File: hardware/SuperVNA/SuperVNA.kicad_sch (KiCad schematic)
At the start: 55 parts, among them Q101 2N2222, Q102 2N2222, U101 LM324, U102 AD626, U103 AD626, U104 SN74CBT3253, U105 SN74CBT3253

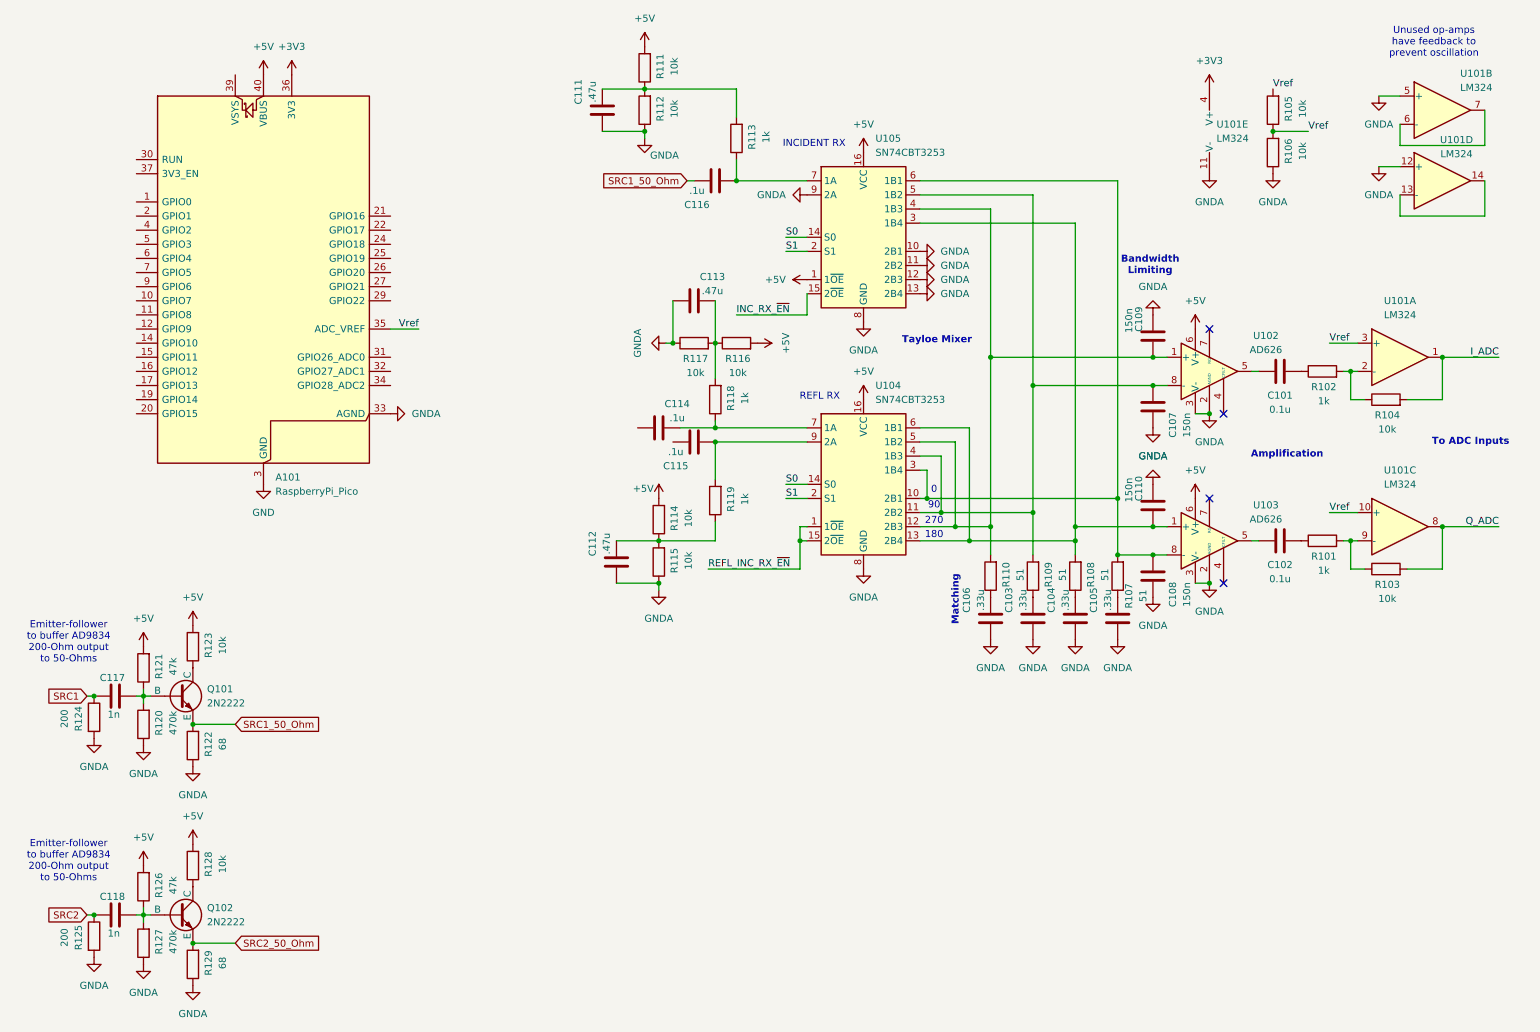
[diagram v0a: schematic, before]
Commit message: deal with the actual frequency used
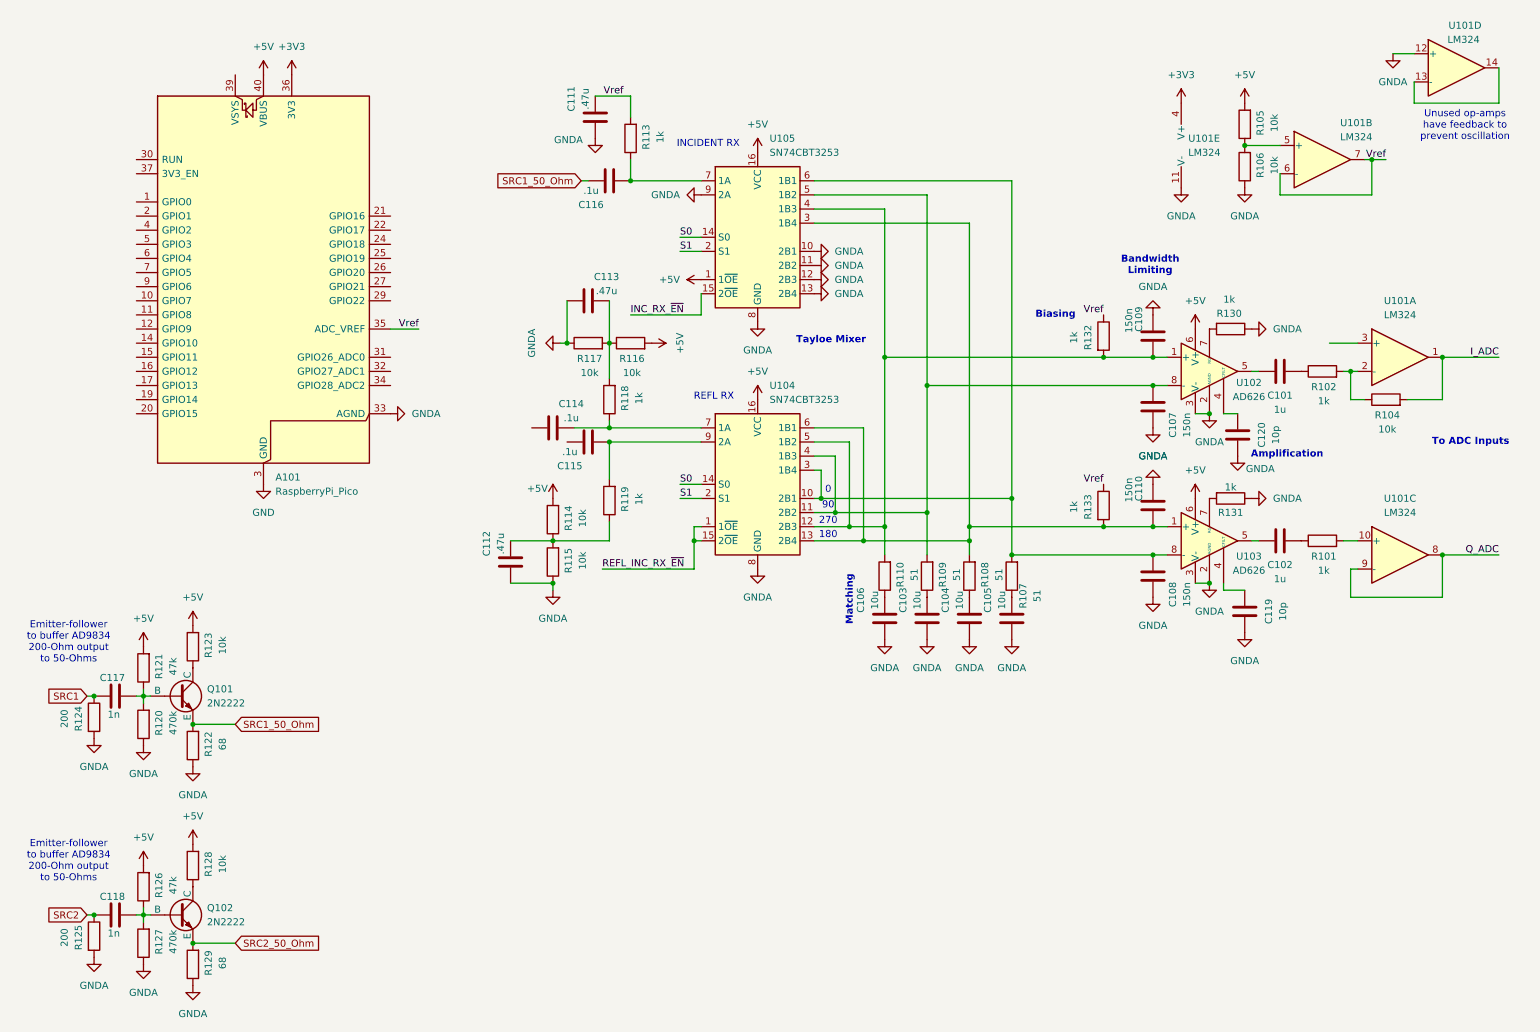
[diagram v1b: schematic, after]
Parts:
- removed R103, R111, R112: 10k, symbol Device:R
- added C119, C120: 10p, symbol Device:C
- added R130, R131, R132, R133: 1k, symbol Device:R
- C101, C102: value 0.1u -> 1u
- C103, C104, C105, C106: value .33u -> 10u
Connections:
- net +5V: now also R105.2
- net GNDA: now also C119.2, C120.2, R130.1, R131.1; no longer U101.5 (+)
- net Q_ADC: now also U101.9 (-)
- net Vref: now also C111.1, R113.2, U101.6 (-), U101.7, R132.1, R133.1; no longer R105.1, R105.2, R106.2, U101.10 (+), U101.3 (+)
- net at C110.1, R108.2, U103.1 (+)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: now also R133.2
- net at U103.4 (CFILT): now also C119.1
- net at U103.7 (RG): now also R131.2
- net at C109.1, R110.2, U102.1 (+)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: now also R132.2
- net at U102.4 (CFILT): now also C120.1
- net at U102.7 (RG): now also R130.2
- net at R101.2: now also U101.10 (+); no longer U101.9 (-)
- new net: R105.1, R106.2, U101.5 (+)
- no-connect marks 4 -> 0
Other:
- note added: "Biasing"
- moved on the sheet: C103, C104, C105, C106, C111, C112, C113, C114, C115, C116, R105, R106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

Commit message: Updated schematic
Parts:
- removed C101, C102: 1u, symbol Device:C
- removed C103, C104, C105, C106: 10u, symbol Device:C
- removed C107, C108, C109, C110: 150n, symbol Device:C
- removed C111, C112, C113: .47u, symbol Device:C
- removed C114, C115, C116: .1u, symbol Device:C
- removed C117, C118: 1n, symbol Device:C
- removed C119, C120: 10p, symbol Device:C
- removed Q101, Q102: 2N2222, symbol Simulation_SPICE:NPN
- removed R101, R102, R113, R118, R119, R130, R131, R132, R133: 1k, symbol Device:R
- removed R104, R105, R106, R114, R115, R116, R117, R123, R128: 10k, symbol Device:R
- removed R107, R108, R109, R110: 51, symbol Device:R
- removed R120, R127: 470k, symbol Device:R
- removed R121, R126: 47k, symbol Device:R
- removed R122, R129: 68, symbol Device:R
- removed R124, R125: 200, symbol Device:R
- removed U101: LM324, symbol Amplifier_Operational:LM324
- removed U102, U103: AD626, symbol AD626:AD626
- removed U104, U105: SN74CBT3253, symbol Analog_Switch:SN74CBT3253
- added D1, D2: LED, symbol Device:LED
- added FB1: FerriteBead, symbol Device:FerriteBead
- added R1: 1k, symbol Device:R
- added U1: AD9834 Module, symbol AD626:AD9834_Module
- added U2: Adafruit TFT Touchscreen LCD, Display:EA_eDIPTFT32-XXX, symbol Display_Graphic:EA_eDIPTFT32-ATP
- renumbered A101 to A1
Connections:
- net +3V3: now also R1.2, U2.2 (VDD), U2.22 (VDD)
- net +5V: now also FB1.1, U1. (Sine_B); no longer A1.40 (VBUS)
- net GND: now also U2.1 (GND), U2.21 (GND), U2.38 (IN6/MI3), U2.39 (IN7/MI2), U2.40 (IN8/MI1)
- net GNDA: now also U1. (Sine_B)
- net LCD_RST: now reaches A1.10 (GPIO7)
- net LCD_RST: now also U2.5 (~{RESET})
- net SDA: now reaches A1.11 (GPIO8)
- net SDA: now also U2.14 (SDA)
- net SCL: now reaches A1.12 (GPIO9)
- net SCL: now also U2.15 (SCL)
- net LCD_SCK: now reaches A1.15 (GPIO11)
- net LCD_SCK: now also U2. (SCK)
- net LCD_MOSI: now reaches A1.16 (GPIO12)
- net LCD_MOSI: now also U2. (SCK)
- net LCD_DC: now reaches A1.17 (GPIO13)
- net LCD_DC: now also U2.18 (DNC)
- net RFL_E: now reaches A1.19 (GPIO14)
- net RFL_E: now also D1.1 (K)
- net at A1.2 (GPIO1): now also U1. (Sine_B)
- net REF_E: now reaches A1.20 (GPIO15)
- net REF_E: now also D2.1 (K)
- net at A1.21 (GPIO16): now also U1. (Sine_B)
- net Analog Electronics/S0: now reaches A1.25 (GPIO19)
- net Analog Electronics/S1: now reaches A1.26 (GPIO20)
- net at A1.27 (GPIO21): now also U1. (Sine_B)
- net ADC_I: now reaches A1.31 (GPIO26_ADC0)
- net ADC_Q: now reaches A1.32 (GPIO27_ADC1)
- net at A1.39 (VSYS): now also FB1.2
- net at A1.5 (GPIO3): now also U1. (Sine_B)
- net at A1.7 (GPIO5): now also U1. (Sine_B)
- net Vref: no longer names the net of A1.35 (ADC_VREF)
- new net: D1.2 (A), D2.2 (A), R1.1
- new net Analog Electronics/SRC1: U1. (Sine_B)
- new net Analog Electronics/SRC2: U1. (Sine_B)
- no-connect marks 0 -> 42
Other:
- added sheet Analog Electronics (analog.kicad_sch)
- note added: "Shows which (if any) receiver input is currently selected."
- note removed: "0"
- note removed: "180"
- note removed: "270"
- note removed: "90"
- note removed: "Amplification"
- note removed: "Bandwidth Limiting"
- note removed: "Biasing"
- note removed: "Emitter-follower to buffer AD9834 200-Ohm output to 50-Ohms"
- note removed: "INCIDENT RX"
- note removed: "Matching"
- note removed: "REFL RX"
- note removed: "Tayloe Mixer"
- note removed: "To ADC Inputs"
- note removed: "Unused op-amps have feedback to prevent oscillation"
- company: (none) -> Lafayette College
- title: (none) -> Super VNA
- moved on the sheet: A1
